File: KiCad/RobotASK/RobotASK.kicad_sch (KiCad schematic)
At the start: 13 parts, among them J1 Conn_01x04_Pin, J2 Conn_01x04_Pin, J3 Conn_01x04_Pin, J4 Conn_01x04_Pin, J5 Conn_01x04_Pin, J6 Conn_01x04_Pin, J7 Conn_01x02_Pin, SW2 SW_Omron_B3FS, U1 ATmega328-P, Y1 16MHz

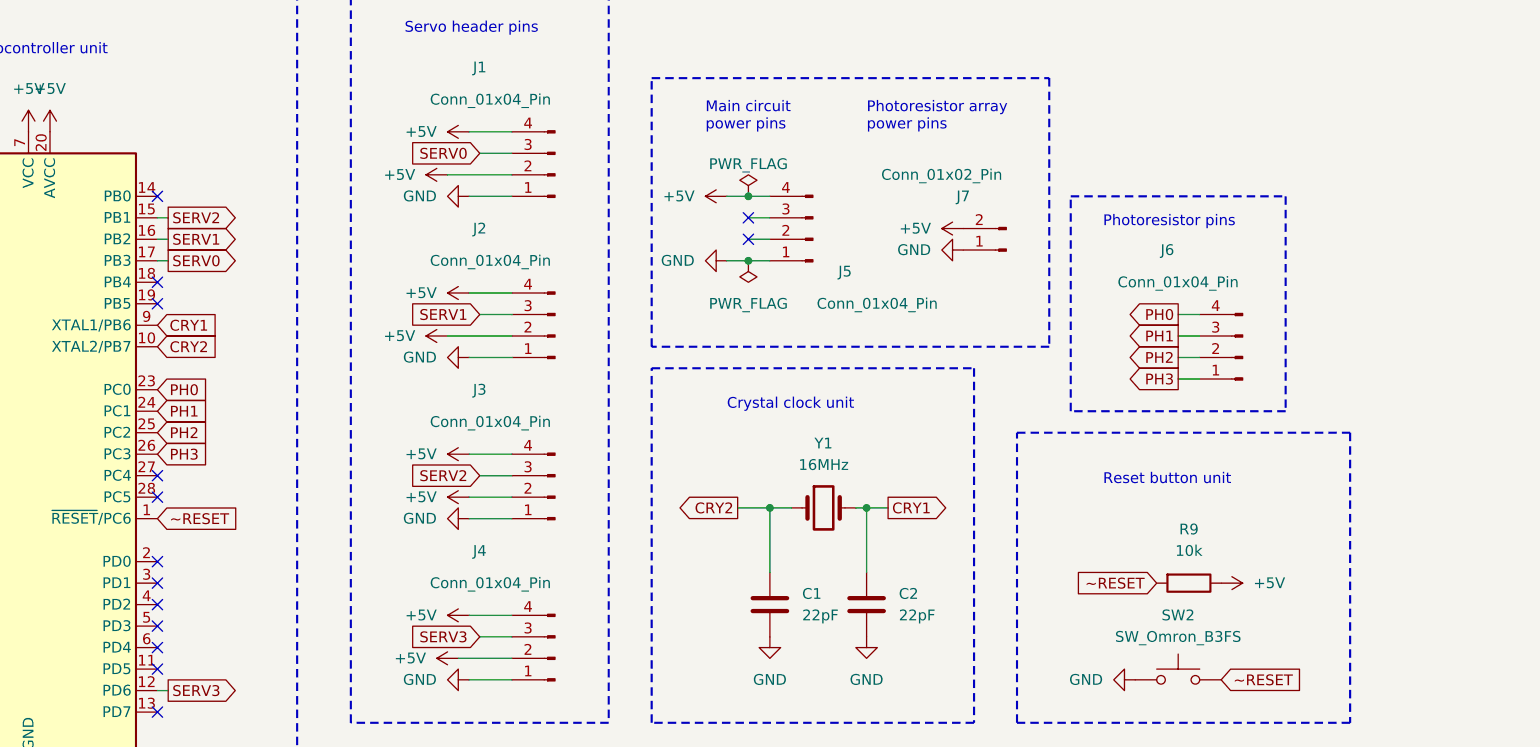
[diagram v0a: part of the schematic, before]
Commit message: Add pins to quickly reprogram the microprocessor
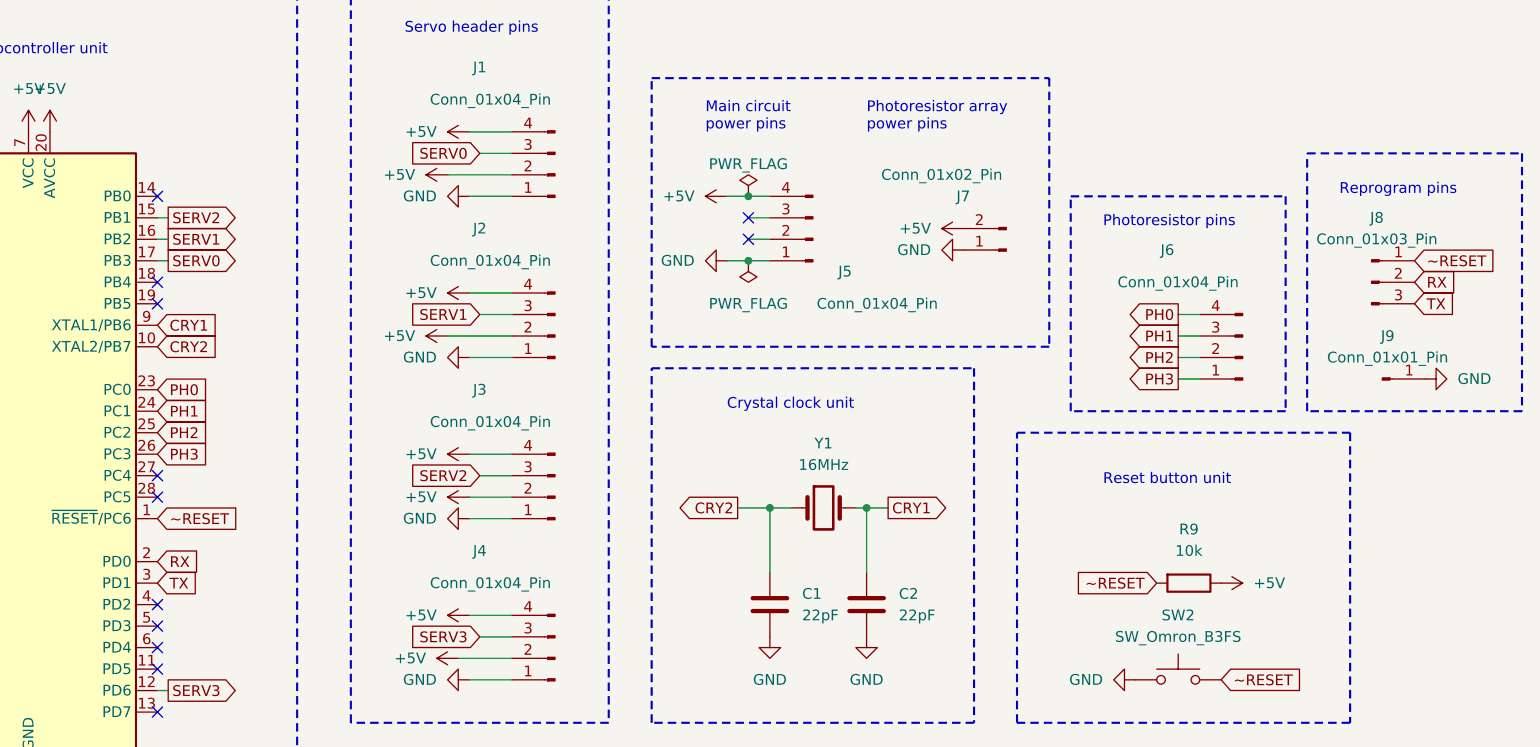
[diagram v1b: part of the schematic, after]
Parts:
- added J8: Conn_01x03_Pin, Connector_PinHeader_2.54mm:PinHeader_1x03_P2.54mm_Vertical, symbol Connector:Conn_01x03_Pin
- added J9: Conn_01x01_Pin, Connector_PinHeader_2.54mm:PinHeader_1x01_P2.54mm_Vertical, symbol Connector:Conn_01x01_Pin
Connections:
- net GND: now also J9.1 (Pin_1)
- net ~RESET: now also J8.1 (Pin_1)
- net RX: now reaches U1.2 (PD0)
- net RX: now also J8.2 (Pin_2)
- net TX: now reaches U1.3 (PD1)
- net TX: now also J8.3 (Pin_3)
- no-connect marks 14 -> 12
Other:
- note added: "Reprogram pins"
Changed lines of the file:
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@@
   (junction (at 146.05 101.6) (diameter 0) (color 0 0 0 0)
   )
-  (no_connect (at 73.66 110.49))
   (no_connect (at 73.66 113.03))
   (no_connect (at 73.66 120.65))
@@
   (no_connect (at 73.66 64.77))
   (no_connect (at 73.66 97.79))
-  (no_connect (at 73.66 107.95))
   (no_connect (at 73.66 77.47))
   (wire (pts (xy 140.97 72.39) (xy 143.51 72.39))
@@
   (wire (pts (xy 110.49 57.15) (xy 115.57 57.15))
     (stroke (width 0) (type default))
+  )
+  (rectangle (start 209.55 59.69) (end 234.95 90.17)
+    (stroke (width 0.25) (type dash))
+    (fill (type none))
   )
   (rectangle (start 132.08 50.8) (end 179.07 82.55)
@@
   )
   (text "Microcontroller unit" (at 50.8 48.26 0)
+    (effects (font (size 1.27 1.27)) (justify left bottom))
+  )
+  (text "Reprogram pins" (at 213.36 64.77 0)
     (effects (font (size 1.27 1.27)) (justify left bottom))
   )
@@
     )
   )
+  (global_label "RX" (shape input) (at 73.66 107.95 0) (fields_autoplaced)
+    (effects (font (size 1.27 1.27)) (justify left))
+    (property "Intersheetrefs" "${INTERSHEET_REFS}" (at 79.1247 107.95 0)
+      (effects (font (size 1.27 1.27)) (justify left) hide)
+    )
+  )
   (global_label "SERV2" (shape input) (at 111.76 97.79 180) (fields_autoplaced)
     (effects (font (size 1.27 1.27)) (justify right))
@@
     )
   )
+  (global_label "~RESET" (shape input) (at 222.25 72.39 0) (fields_autoplaced)
+    (effects (font (size 1.27 1.27)) (justify left))
+    (property "Intersheetrefs" "${INTERSHEET_REFS}" (at 231.8874 72.39 0)
+      (effects (font (size 1.27 1.27)) (justify left) hide)
+    )
+  )
   (global_label "SERV0" (shape input) (at 111.76 59.69 180) (fields_autoplaced)
     (effects (font (size 1.27 1.27)) (justify right))
@@
     )
   )
+  (global_label "TX" (shape input) (at 222.25 77.47 0) (fields_autoplaced)
+    (effects (font (size 1.27 1.27)) (justify left))
+    (property "Intersheetrefs" "${INTERSHEET_REFS}" (at 227.4123 77.47 0)
+      (effects (font (size 1.27 1.27)) (justify left) hide)
+    )
+  )
   (global_label "SERV3" (shape output) (at 74.93 123.19 0) (fields_autoplaced)
     (effects (font (size 1.27 1.27)) (justify left))
@@
     (effects (font (size 1.27 1.27)) (justify left))
     (property "Intersheetrefs" "${INTERSHEET_REFS}" (at 80.4552 90.17 0)
+      (effects (font (size 1.27 1.27)) (justify left) hide)
+    )
+  )
+  (global_label "RX" (shape input) (at 222.25 74.93 0) (fields_autoplaced)
+    (effects (font (size 1.27 1.27)) (justify left))
+    (property "Intersheetrefs" "${INTERSHEET_REFS}" (at 227.7147 74.93 0)
       (effects (font (size 1.27 1.27)) (justify left) hide)
     )
@@
     )
   )
+  (global_label "TX" (shape input) (at 73.66 110.49 0) (fields_autoplaced)
+    (effects (font (size 1.27 1.27)) (justify left))
+    (property "Intersheetrefs" "${INTERSHEET_REFS}" (at 78.8223 110.49 0)
+      (effects (font (size 1.27 1.27)) (justify left) hide)
+    )
+  )
   (global_label "PH1" (shape output) (at 194.31 81.28 180) (fields_autoplaced)
     (effects (font (size 1.27 1.27)) (justify right))
@@
         (path "/9fd972e4-939b-4c5b-ad22-9d1a67eaf6a2"
           (reference "C2") (unit 1)
+        )
+      )
+    )
+  )
+  (symbol (lib_id "power:GND") (at 223.52 86.36 90) (unit 1)
+    (in_bom yes) (on_board yes) (dnp no) (fields_autoplaced)
+    (property "Reference" "#PWR025" (at 229.87 86.36 0)
+      (effects (font (size 1.27 1.27)) hide)
+    )
+    (property "Value" "GND" (at 227.33 86.36 90)
+      (effects (font (size 1.27 1.27)) (justify right))
+    )
+    (property "Footprint" "" (at 223.52 86.36 0)
+      (effects (font (size 1.27 1.27)) hide)
+    )
+    (property "Datasheet" "" (at 223.52 86.36 0)
+      (effects (font (size 1.27 1.27)) hide)
+    )
+    (pin "1")
+    (instances
+      (project "RobotASK"
+        (path "/9fd972e4-939b-4c5b-ad22-9d1a67eaf6a2"
+          (reference "#PWR025") (unit 1)
         )
       )
@@
     )
   )
+  (symbol (lib_id "Connector:Conn_01x01_Pin") (at 218.44 86.36 0) (unit 1)
+    (in_bom yes) (on_board yes) (dnp no) (fields_autoplaced)
+    (property "Reference" "J9" (at 219.075 81.28 0)
+      (effects (font (size 1.27 1.27)))
+    )
+    (property "Value" "Conn_01x01_Pin" (at 219.075 83.82 0)
+      (effects (font (size 1.27 1.27)))
+    )
+    (property "Footprint" "Connector_PinHeader_2.54mm:PinHeader_1x01_P2.54mm_Vertical" (at 218.44 86.36 0)
+      (effects (font (size 1.27 1.27)) hide)
+    )
+    (property "Datasheet" "~" (at 218.44 86.36 0)
+      (effects (font (size 1.27 1.27)) hide)
+    )
+    (pin "1")
+    (instances
+      (project "RobotASK"
+        (path "/9fd972e4-939b-4c5b-ad22-9d1a67eaf6a2"
+          (reference "J9") (unit 1)
+        )
+      )
+    )
+  )
   (symbol (lib_id "power:+5V") (at 109.22 119.38 90) (unit 1)
     (in_bom yes) (on_board yes) (dnp no) (fields_autoplaced)
@@
         )
       )
+    )
+  )
+  (symbol (lib_id "Connector:Conn_01x03_Pin") (at 217.17 74.93 0) (unit 1)
+    (in_bom yes) (on_board yes) (dnp no) (fields_autoplaced)
+    (property "Reference" "J8" (at 217.805 67.31 0)
+      (effects (font (size 1.27 1.27)))
+    )
+    (property "Value" "Conn_01x03_Pin" (at 217.805 69.85 0)
+      (effects (font (size 1.27 1.27)))
+    )
+    (property "Footprint" "Connector_PinHeader_2.54mm:PinHeader_1x03_P2.54mm_Vertical" (at 217.17 74.93 0)
+      (effects (font (size 1.27 1.27)) hide)
+    )
+    (property "Datasheet" "~" (at 217.17 74.93 0)
+      (effects (font (size 1.27 1.27)) hide)
+    )
+    (pin "3")
+    (pin "2")
+    (pin "1")
+    (instances
+      (project "RobotASK"
+        (path "/9fd972e4-939b-4c5b-ad22-9d1a67eaf6a2"
+          (reference "J8") (unit 1)
+        )
+      )

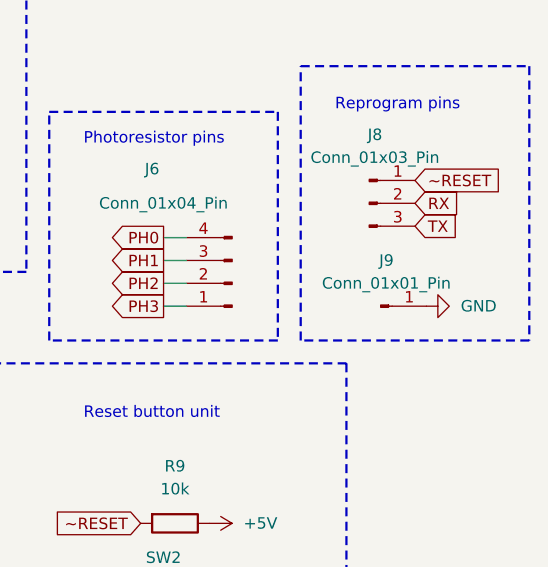
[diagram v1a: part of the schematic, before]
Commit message: Bez zbędnego pinu GND, update KiCad 8, export ze ścieżkami
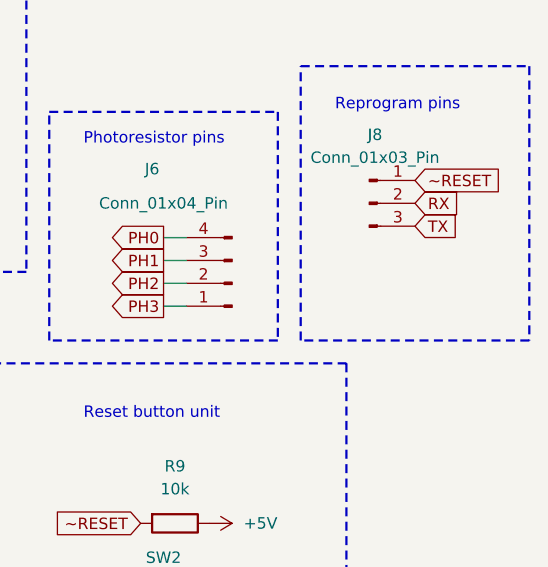
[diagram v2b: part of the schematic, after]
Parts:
- removed J9: Conn_01x01_Pin, Connector_PinHeader_2.54mm:PinHeader_1x01_P2.54mm_Vertical, symbol Connector:Conn_01x01_Pin

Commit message: renders
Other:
- moved on the sheet: C1, C2, J1, J2, J3, J4, J5, J6, J7, J8, R9, SW2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
